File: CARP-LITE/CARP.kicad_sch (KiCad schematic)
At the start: 110 parts, among them J1 USB-C, J10 PYRO_2, J3 I2C1+3V3, J4 2S XT30, J5 UART+5V+I2C1, J6 PYRO_1, J8 PWM1+5V1, J9 PWM2+5V1, Q5 SQ2318CES, Q6 SQ2318CES, Q7 SQ2318CES, SW1 SW_Push, SW2 SW_Push, U1 W25Q128JVSIMTR (16MB), U10 TPS62130A, U2 W25Q32RVXHJQ (2MB), U4 RP2350_60QFN, U5 LSM6DSO, U6 BMP390, U7 TLV75733PDBV, Y1 ABM8-272-T3

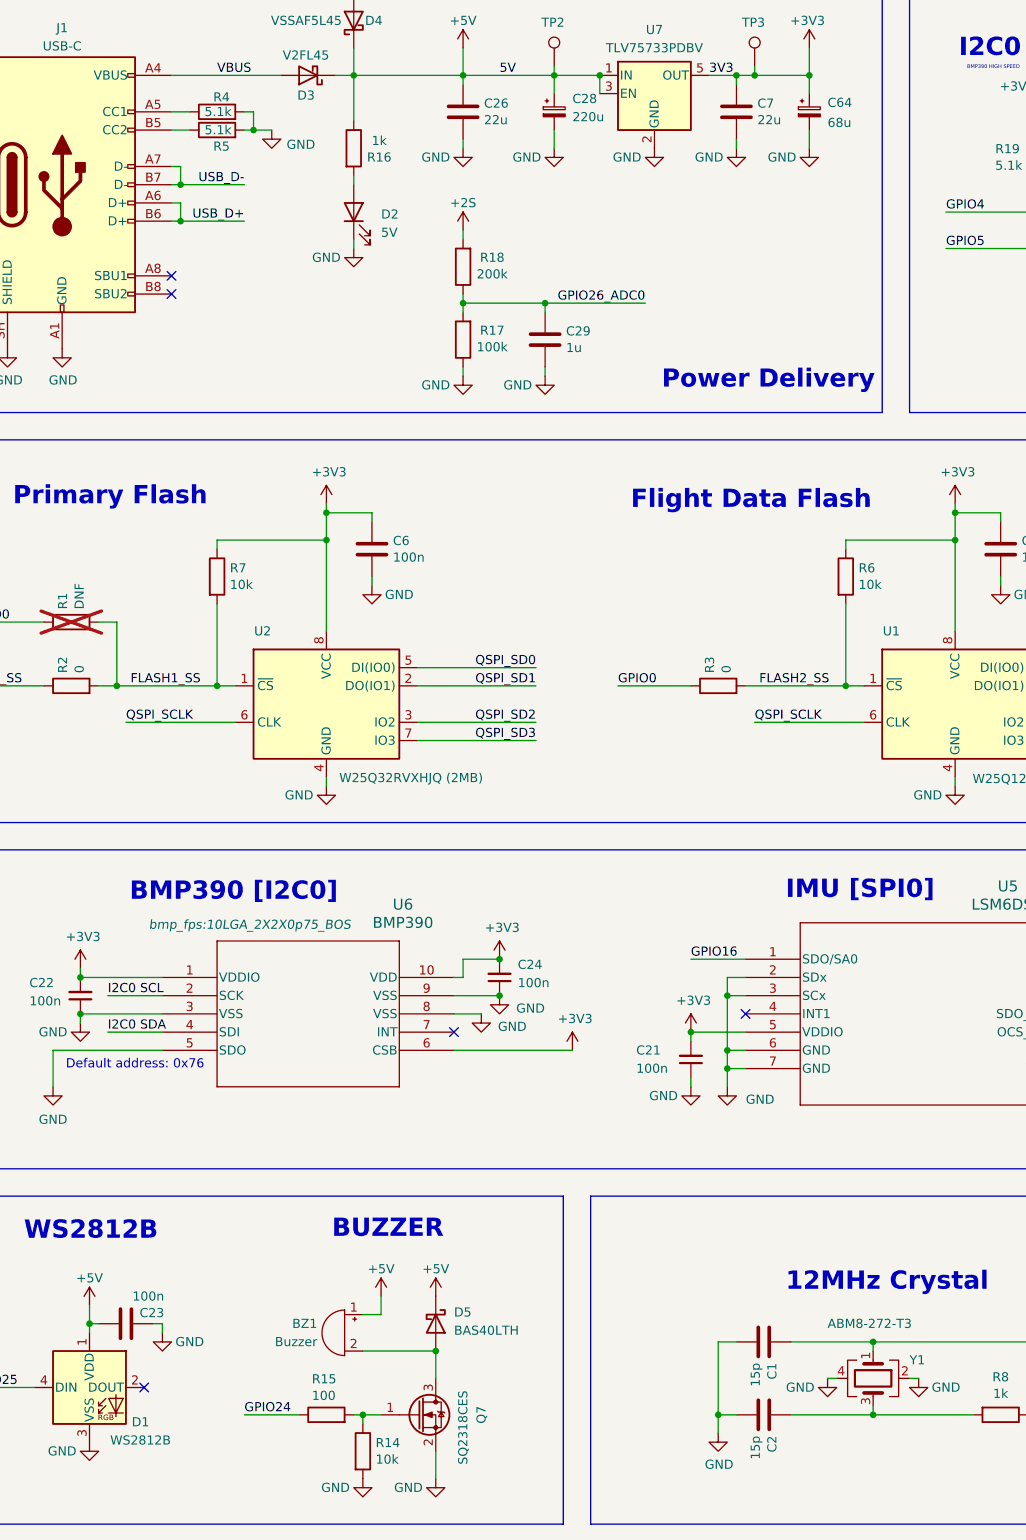
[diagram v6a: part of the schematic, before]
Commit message: change sizes
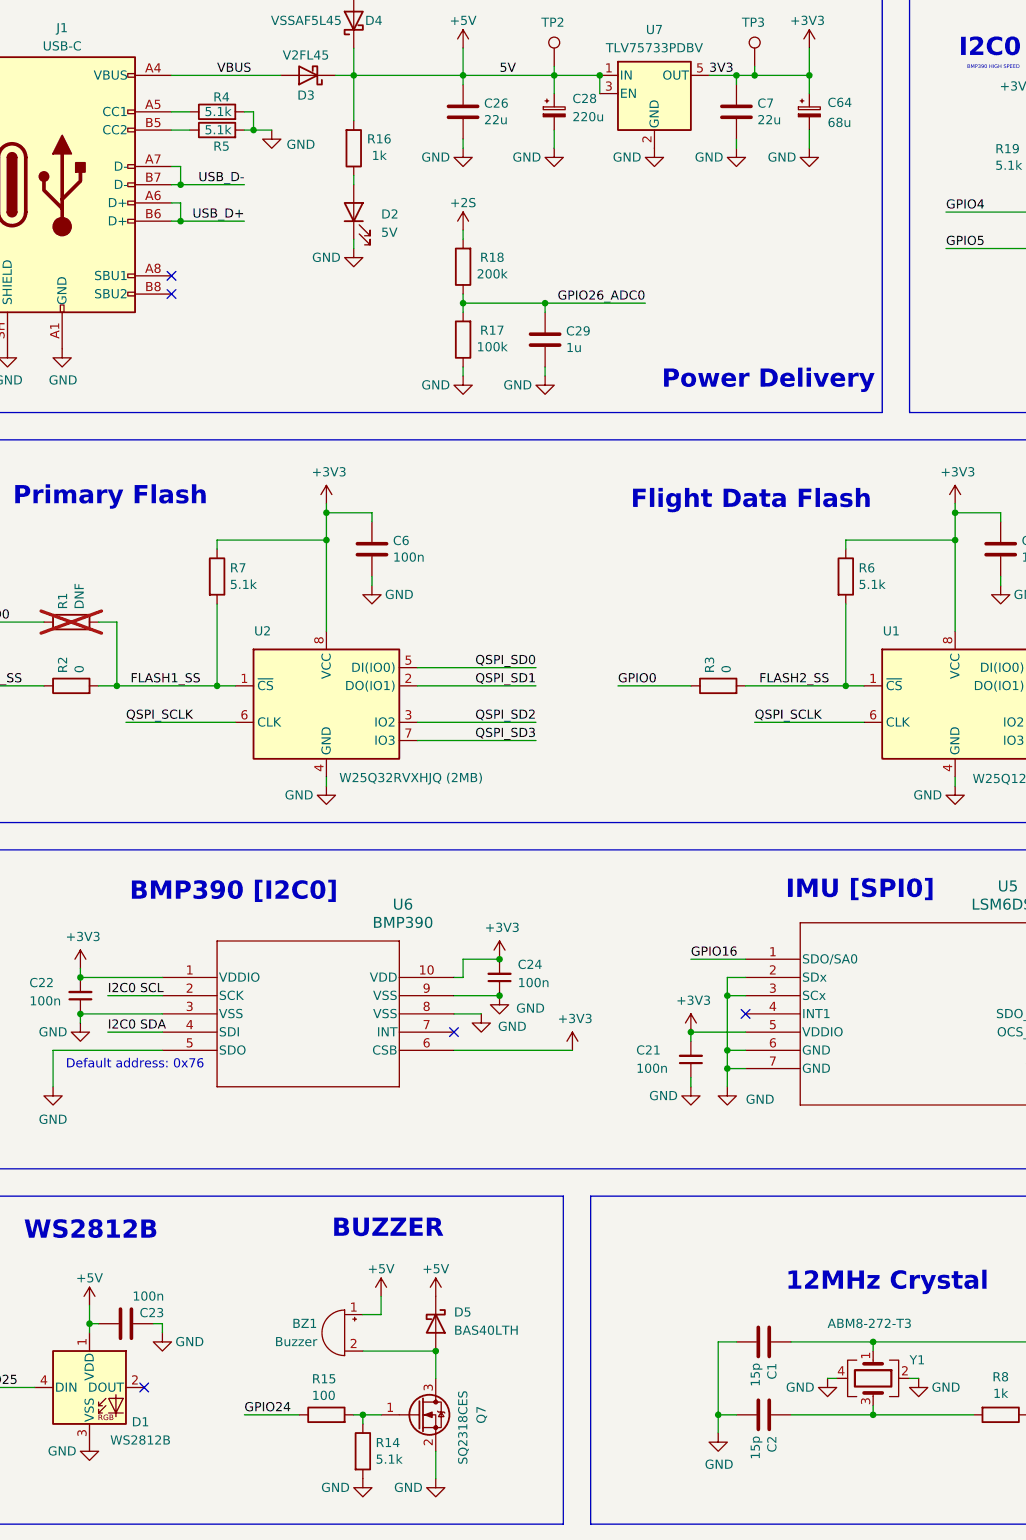
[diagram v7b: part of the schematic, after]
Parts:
- R11, R16, R9: footprint Resistor_SMD:R_0603_1608Metric -> Resistor_SMD:R_0402_1005Metric
- R14, R6, R7: value 10k -> 5.1k; footprint Resistor_SMD:R_0603_1608Metric -> Resistor_SMD:R_0402_1005Metric
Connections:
- net +5V: now also R16.2; no longer R16.1
- net at D2.2 (A): now also R16.1; no longer R16.2
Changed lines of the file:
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@@
 	)
 	(junction
+		(at 105.41 81.28)
+		(diameter 0)
+		(color 0 0 0 0)
+	)
+	(junction
 		(at 342.9 237.49)
 		(diameter 0)
@@
 	)
 	(junction
-		(at 105.41 81.28)
-		(diameter 0)
-		(color 0 0 0 0)
-	)
-	(junction
 		(at 284.48 43.18)
 		(diameter 0)
@@
 			)
 		)
-		(property "Footprint" "Resistor_SMD:R_0603_1608Metric"
+		(property "Footprint" "Resistor_SMD:R_0402_1005Metric"
 			(at 240.03 125.222 90)
 			(hide yes)
@@
 			)
 		)
-		(property "Footprint" "Resistor_SMD:R_0603_1608Metric"
+		(property "Footprint" "Resistor_SMD:R_0402_1005Metric"
 			(at 250.825 83.312 90)
 			(hide yes)
@@
 		(lib_id "Device:R")
 		(at 71.12 91.44 0)
+		(mirror x)
 		(unit 1)
 		(body_style 1)
@@
 		(dnp no)
 		(property "Reference" "R16"
-			(at 74.676 92.71 0)
+			(at 74.676 90.17 0)
 			(show_name no)
 			(do_not_autoplace no)
@@
 		)
 		(property "Value" "1k"
-			(at 74.676 90.3986 0)
+			(at 74.676 92.4814 0)
 			(show_name no)
 			(do_not_autoplace no)
@@
 			)
 		)
-		(property "Footprint" "Resistor_SMD:R_0603_1608Metric"
+		(property "Footprint" "Resistor_SMD:R_0402_1005Metric"
 			(at 69.342 91.44 90)
 			(hide yes)
@@
 			)
 		)
-		(property "Value" "10k"
+		(property "Value" "5.1k"
 			(at 141.478 152.273 0)
 			(show_name no)
@@
 			)
 		)
-		(property "Footprint" "Resistor_SMD:R_0603_1608Metric"
+		(property "Footprint" "Resistor_SMD:R_0402_1005Metric"
 			(at 137.922 151.13 90)
 			(hide yes)
@@
 		(property "Footprint" "bmp_fps:10LGA_2X2X0p75_BOS"
 			(at 56.642 199.644 0)
+			(hide yes)
 			(show_name no)
 			(do_not_autoplace no)
@@
 			)
 		)
-		(property "Value" "10k"
+		(property "Value" "5.1k"
 			(at 74.168 274.193 0)
 			(show_name no)
@@
 			)
 		)
-		(property "Footprint" "Resistor_SMD:R_0603_1608Metric"
+		(property "Footprint" "Resistor_SMD:R_0402_1005Metric"
 			(at 70.612 273.05 90)
 			(hide yes)
@@
 			)
 		)
-		(property "Value" "10k"
+		(property "Value" "5.1k"
 			(at 53.848 152.273 0)
 			(show_name no)
@@
 			)
 		)
-		(property "Footprint" "Resistor_SMD:R_0603_1608Metric"
+		(property "Footprint" "Resistor_SMD:R_0402_1005Metric"
 			(at 50.292 151.13 90)
 			(hide yes)

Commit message: change more sizes
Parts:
- R23: footprint Resistor_SMD:R_0603_1608Metric -> Resistor_SMD:R_0402_1005Metric
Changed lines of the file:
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@@
 			)
 		)
-		(property "Footprint" "Resistor_SMD:R_0603_1608Metric"
+		(property "Footprint" "Resistor_SMD:R_0402_1005Metric"
 			(at 69.85 45.72 0)
 			(hide yes)
